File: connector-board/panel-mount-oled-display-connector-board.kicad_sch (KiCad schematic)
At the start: 3 parts, among them J1 Conn_01x08_Pin, J2 Conn_01x08_Pin, J3 Conn_01x16_Socket

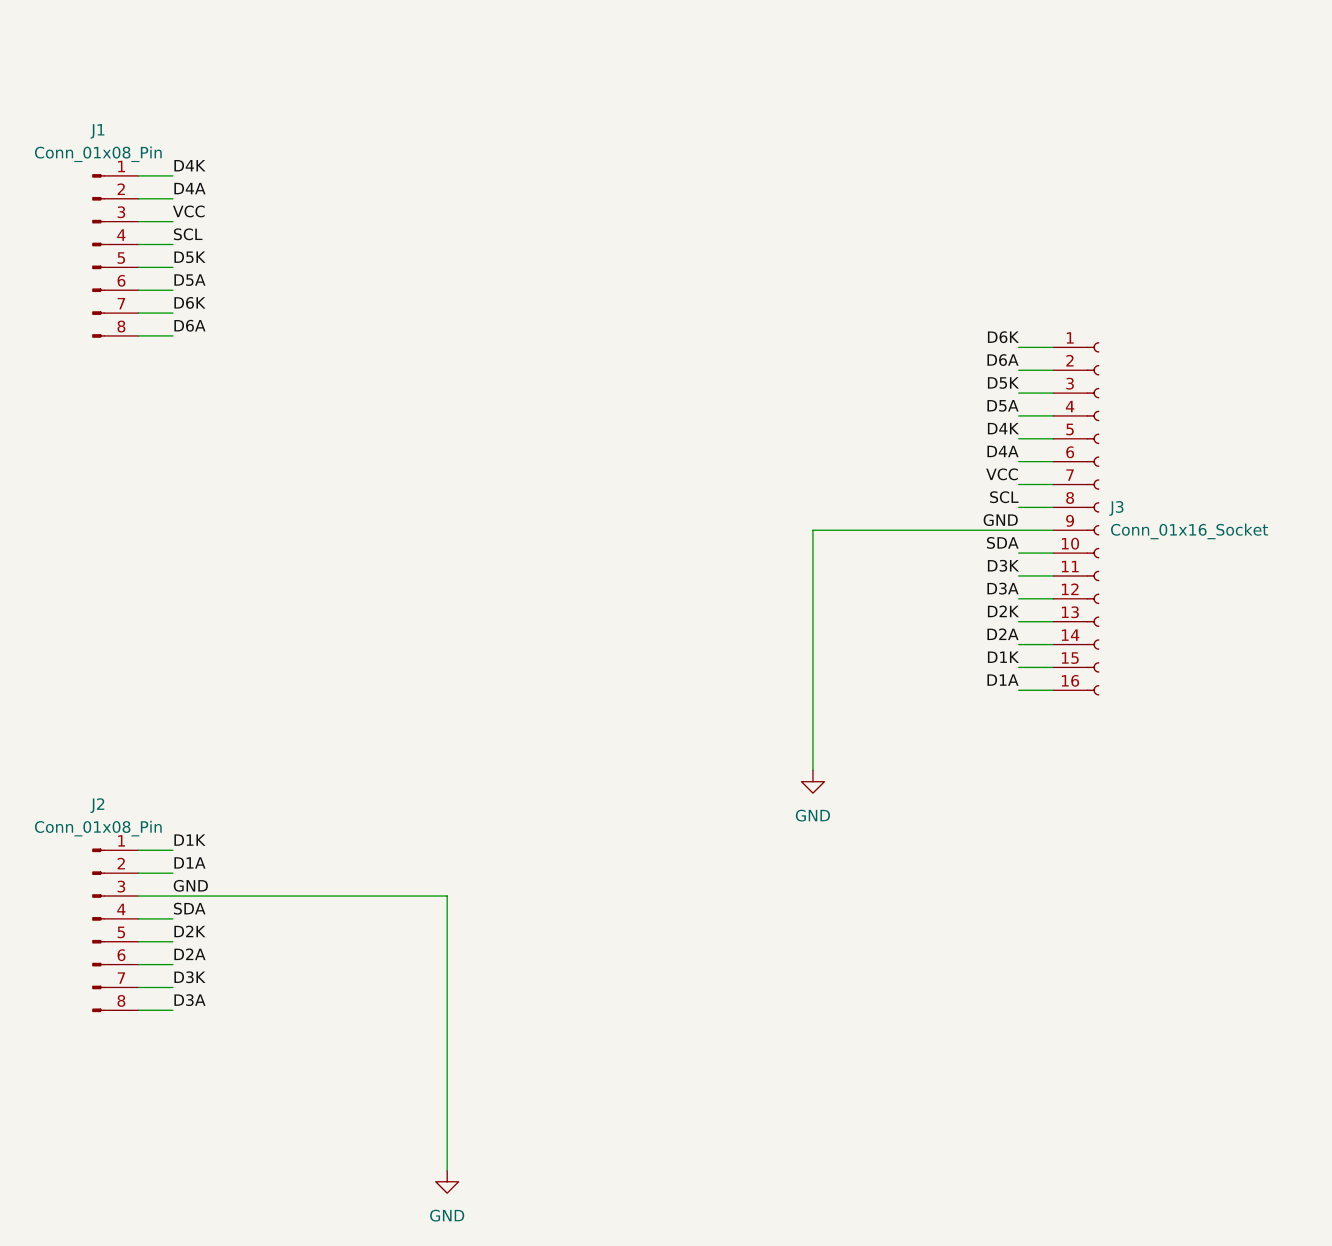
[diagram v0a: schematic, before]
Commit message: connector: add dual screw-terminal connector options
Add a new connector on the connector board to support either
single-level or two-level screw terminal blocks, providing
flexibility to expose more LEDs when needed.
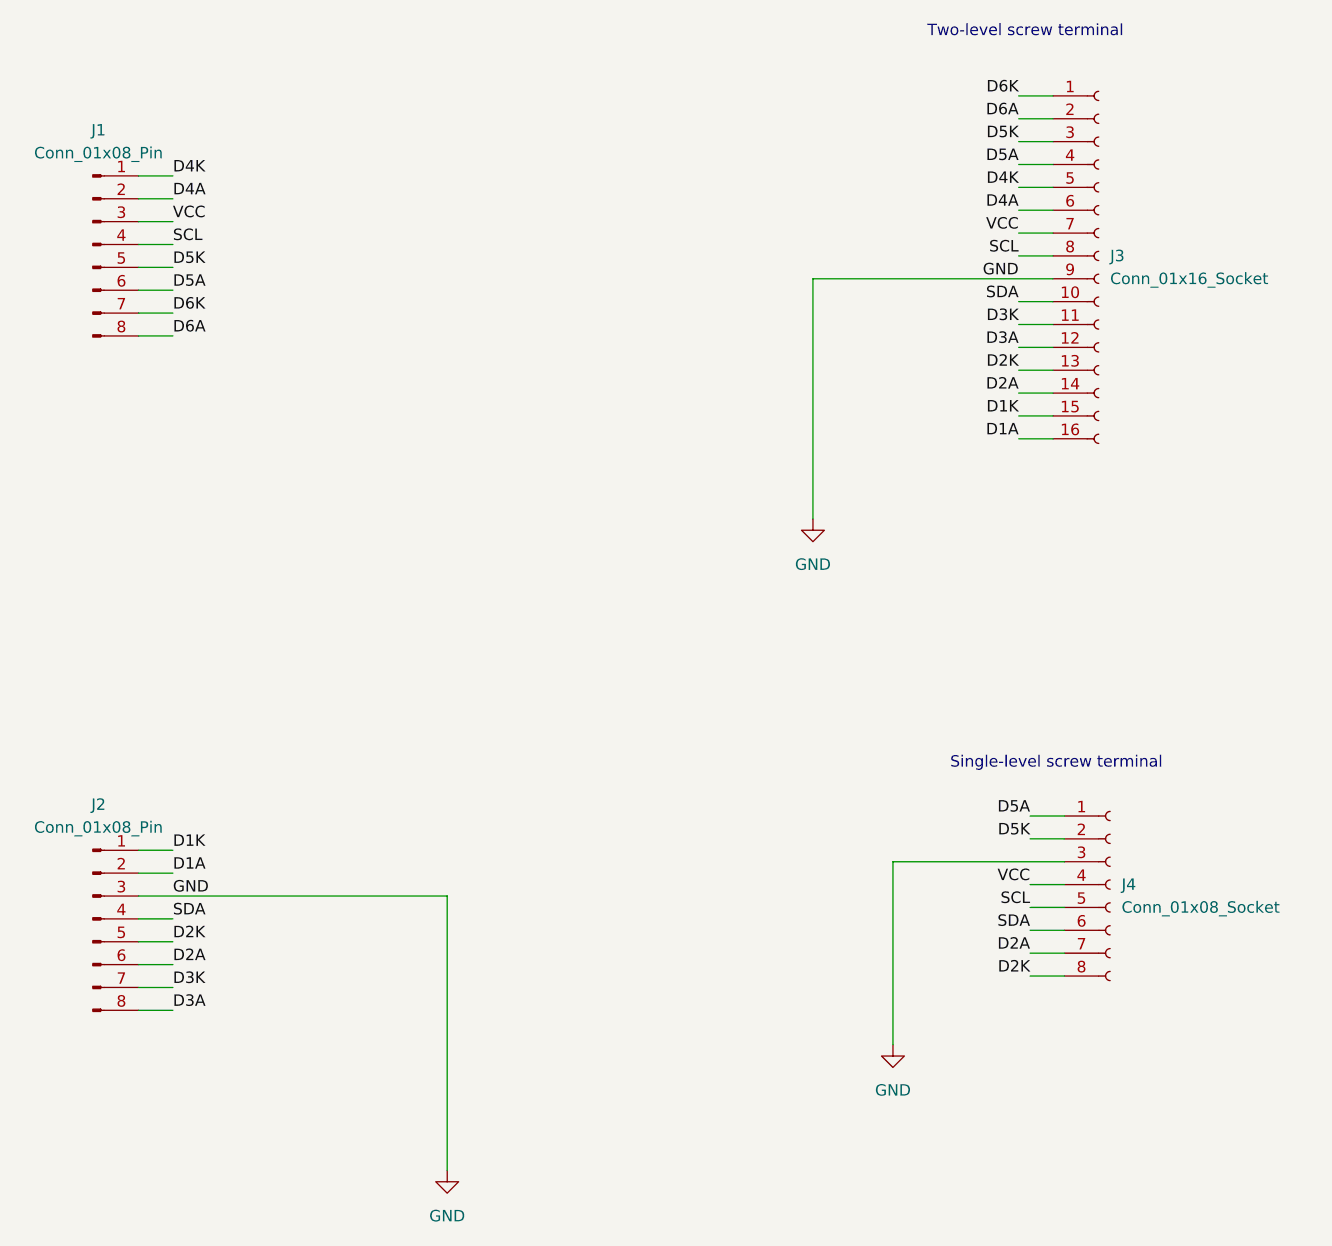
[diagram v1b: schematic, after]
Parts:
- added J4: Conn_01x08_Socket, TerminalBlock_4Ucon:TerminalBlock_4Ucon_1x08_P3.50mm_Horizontal, symbol Connector:Conn_01x08_Socket
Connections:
- net D2A: now also J4.7 (Pin_7)
- net D2K: now also J4.8 (Pin_8)
- net D5A: now also J4.1 (Pin_1)
- net D5K: now also J4.2 (Pin_2)
- net GND: now also J4.3 (Pin_3)
- net SCL: now also J4.5 (Pin_5)
- net SDA: now also J4.6 (Pin_6)
- net VCC: now also J4.4 (Pin_4)
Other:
- note added: "Single-level screw terminal"
- note added: "Two-level screw terminal"
- moved on the sheet: J3
